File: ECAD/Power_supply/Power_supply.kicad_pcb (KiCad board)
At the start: 2 copper layers, 104 x 127 mm, 52 parts, among them J1 Barrel_Jack_Switch, J2 Conn_01x06, Q1 DMP3037LSS-13, SW1 SW_Push_DPDT, U1 LM317_TO-220, U2 LM317_TO-220, U3 LM317_TO-220

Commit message: Progressed ECAD.
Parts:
- moved C5 82.2 mm to (134.6, 153.7), turned to 0 degrees
- moved R2 69.9 mm to (141.0, 145.4), turned to 0 degrees
- moved C4 67.9 mm to (141.0, 142.9), turned to 0 degrees
- moved D6 66.6 mm to (134.6, 148.0)
- moved R5 64.7 mm to (134.6, 142.9), turned to 0 degrees
- moved C2 53.6 mm to (133.3, 136.5), turned to 90 degrees
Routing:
- net /ADJ_9V: track 18.4 -> 13.3 mm
- net GND: vias 14 -> 18
- added copper zone on F.Cu, net /ADJ_9V

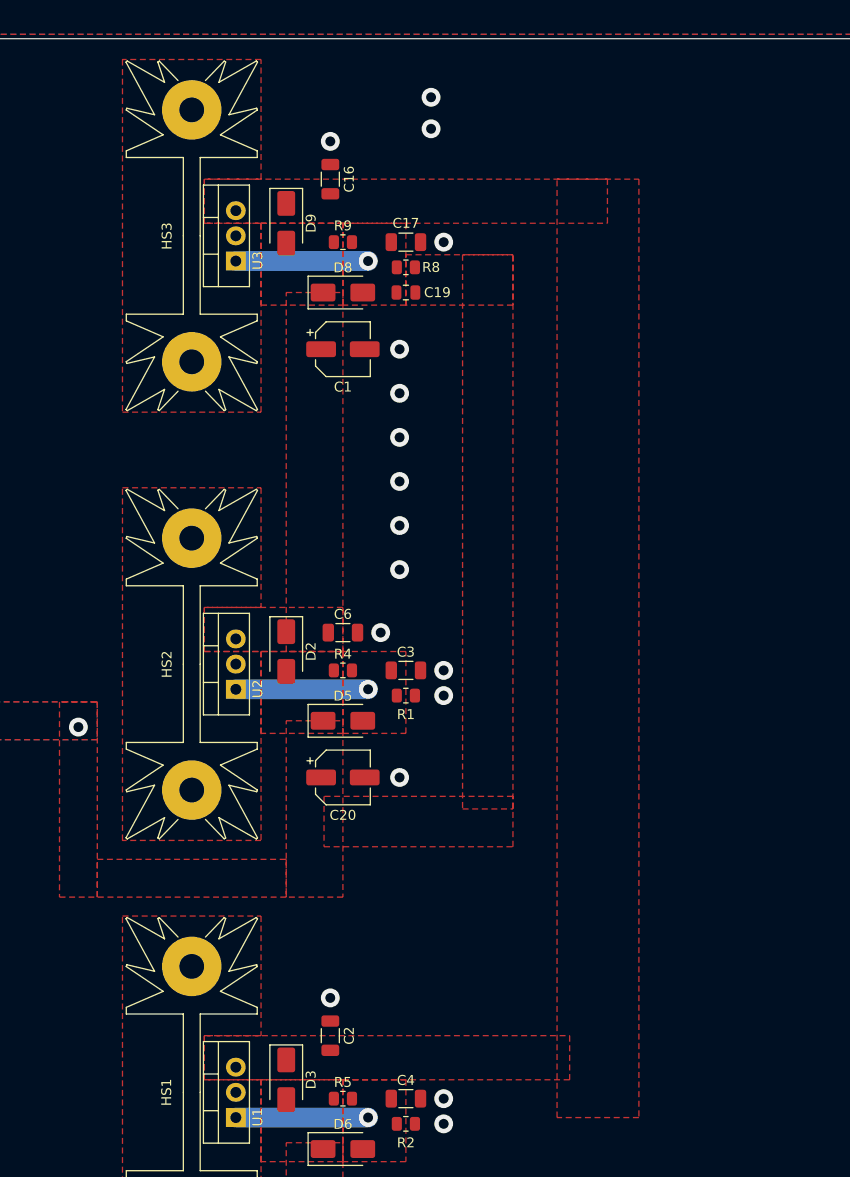
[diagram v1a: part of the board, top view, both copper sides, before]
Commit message: Improved layout.
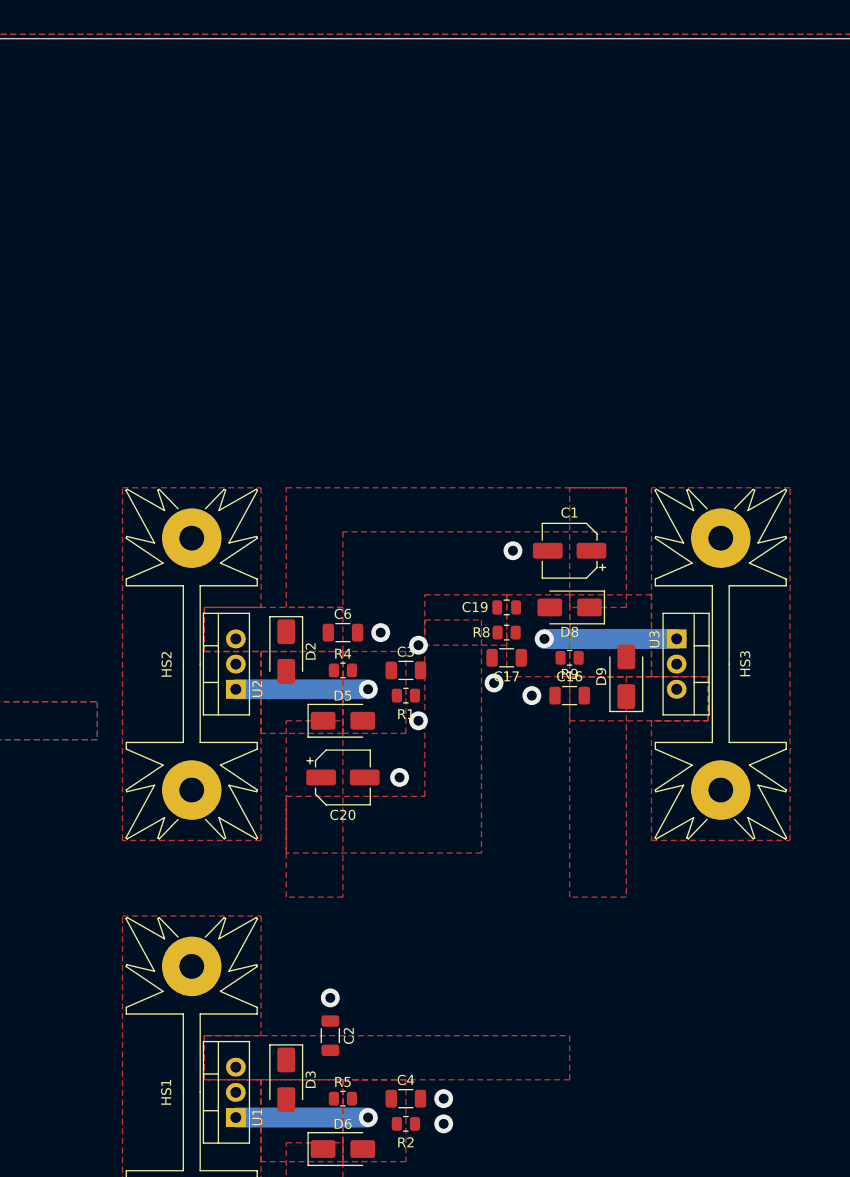
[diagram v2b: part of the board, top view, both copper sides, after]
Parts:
- moved HS3 68.6 mm to (172.7, 99.1), turned to -90 degrees
- moved U3 58.5 mm to (168.3, 96.5), turned to -90 degrees
- moved C16 57.4 mm to (157.5, 102.2), turned to 180 degrees
- moved D9 57.1 mm to (163.2, 100.3), turned to 90 degrees
- moved R9 47.7 mm to (157.5, 98.4), turned to 180 degrees
- moved C17 43.1 mm to (151.1, 98.4), turned to 180 degrees
- moved D8 39.1 mm to (157.5, 93.3), turned to 180 degrees
- moved R8 38.2 mm to (151.1, 95.9), turned to 180 degrees
- moved C19 33.3 mm to (151.1, 93.3), turned to 180 degrees
- moved C1 30.6 mm to (157.5, 87.6), turned to 180 degrees
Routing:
- net GND: vias 18 -> 11
- net +5V: vias 1 -> 0

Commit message: Progressed ECAD.
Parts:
- moved R7 168.3 mm to (168.5, 159.4)
- moved D7 168.3 mm to (160.6, 156.8)
- moved D1 134.1 mm to (169.5, 110.5), turned to 90 degrees
- moved Q1 117.7 mm to (175.9, 110.5), turned to 90 degrees
- moved D4 111.1 mm to (181.3, 114.0), turned to -90 degrees
- moved R3 109.5 mm to (182.9, 108.0), turned to 90 degrees
- moved FL1 102.0 mm to (182.9, 125.0), turned to -90 degrees
- moved J1 77.0 mm to (175.6, 88.9)
- moved SW1 67.3 mm to (177.0, 100.3), turned to 0 degrees
- moved C11 41.1 mm to (216.3, 134.4)
- moved C12 41.1 mm to (216.3, 137.7)
- moved C9 41.1 mm to (215.3, 145.4)
- moved L1 41.1 mm to (250.3, 132.4)
- moved L2 41.1 mm to (242.1, 132.4)
- moved C10 41.1 mm to (229.1, 145.4)
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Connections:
- net Net-(D1-A2) renamed /SW_OUT
- net Net-(J1-Pad1) renamed /SW_IN
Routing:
- net GND: track 0.00 -> 25.0 mm, vias 11 -> 12
- net GNDPWR: vias 0 -> 3
- net +9V: vias 0 -> 1
- net +5V: vias 0 -> 1
- net +12V: vias 0 -> 1
- added copper zone on B.Cu, net +12V
- added copper zone on B.Cu, net +9V
- added copper zone on F.Cu, net /SW_IN
- added copper zone on F.Cu, net /SW_OUT
- added copper zone on B.Cu, net GNDPWR
- removed copper zone on F.Cu, net GND
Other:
- board size 104 x 127 mm -> 95 x 127 mm

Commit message: Progressed PCB
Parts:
- moved L1 78.3 mm to (172.1, 130.6)
- moved R6 72.4 mm to (163.2, 157.5)
- moved C14 62.8 mm to (163.2, 153.0)
- moved C13 62.7 mm to (163.2, 149.2)
- moved L2 61.7 mm to (180.3, 130.8)
- moved C15 60.0 mm to (163.2, 141.6)
- moved C11 54.3 mm to (163.2, 145.4)
- moved C10 53.5 mm to (175.9, 151.8), turned to 180 degrees
- moved C12 53.1 mm to (163.2, 137.8)
- moved C9 39.6 mm to (175.9, 141.0), turned to 180 degrees
- moved D7 31.9 mm to (192.4, 154.3)
- moved R7 28.4 mm to (196.8, 161.3)
- moved FL1 8.25 mm to (175.9, 120.7)
- moved H4 5.08 mm to (180.3, 158.8)
- moved R3 2.01 mm to (182.2, 109.9)
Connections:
- net Net-(D4-K) renamed /PRE_FILTER
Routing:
- net Net-(D4-A): track 0.00 -> 8.32 mm
- net GNDPWR: track 0.00 -> 7.27 mm, vias 3 -> 4
- net GND: track 25.0 -> 26.9 mm
- added copper zone on F.Cu, net /PRE_FILTER

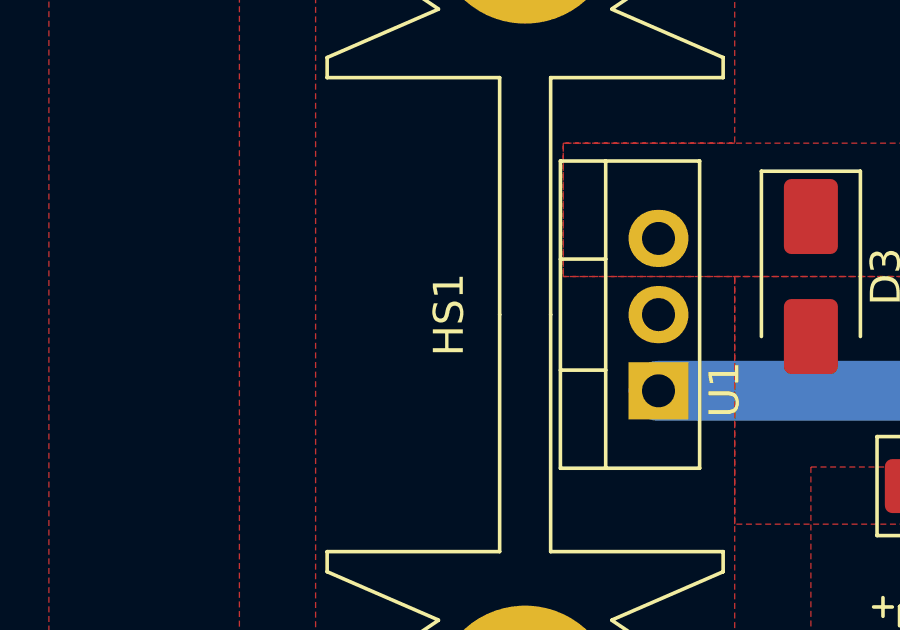
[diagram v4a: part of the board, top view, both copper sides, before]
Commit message: Added heatsink 3D model.
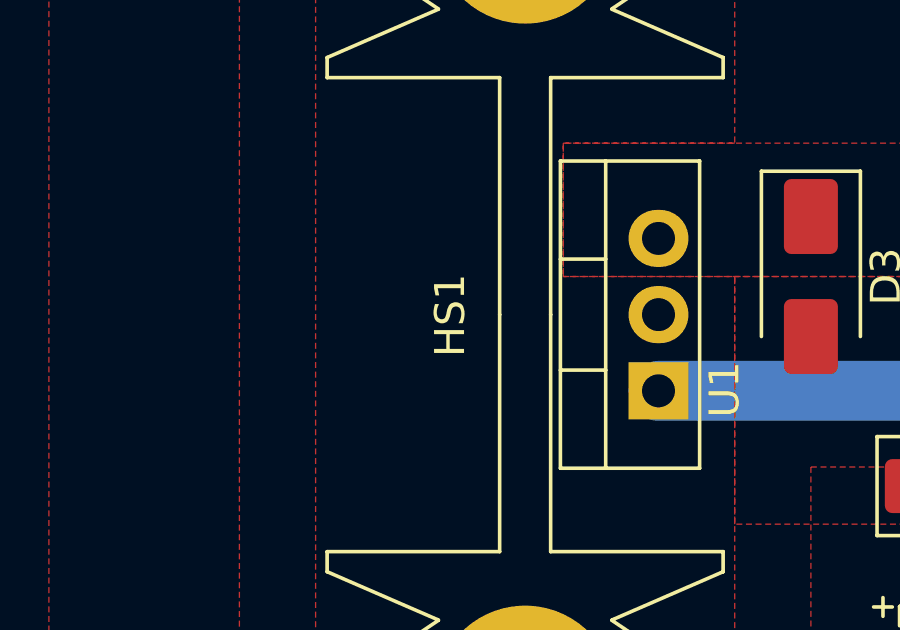
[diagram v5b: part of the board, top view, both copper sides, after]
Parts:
- HS1, HS2, HS3: footprint Heatsink:Heatsink_Fischer_SK104-STC-STIC_35x13mm_2xDrill2.5mm -> Heatsink_custom:Heatsink_Fischer_SK104-STC-STIC_35x13mm_2xDrill2.5mm
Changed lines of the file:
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@@
 		(tags "inductor taiyo-yuden nr smd")
 		(property "Reference" "L1"
-			(at 0 -4 360)
+			(at 0 -4 0)
 			(layer "F.SilkS")
 			(effects
@@
 		)
 		(property "Value" "100uL"
-			(at 0 4.5 360)
+			(at 0 4.5 0)
 			(layer "F.Fab")
 			(effects
@@
 		)
 		(fp_text user "${REFERENCE}"
-			(at 0 0 360)
+			(at 0 0 0)
 			(layer "F.Fab")
 			(effects
@@
 		(tags "inductor taiyo-yuden nr smd")
 		(property "Reference" "L2"
-			(at 0 -2.5 360)
+			(at 0 -2.5 0)
 			(layer "F.SilkS")
 			(effects
@@
 		)
 		(property "Value" "10uL"
-			(at 0 3 360)
+			(at 0 3 0)
 			(layer "F.Fab")
 			(effects
@@
 		)
 		(fp_text user "${REFERENCE}"
-			(at 0 0 360)
+			(at 0 0 0)
 			(layer "F.Fab")
 			(effects
@@
 		)
 	)
-	(footprint "Heatsink:Heatsink_Fischer_SK104-STC-STIC_35x13mm_2xDrill2.5mm"
+	(footprint "Heatsink_custom:Heatsink_Fischer_SK104-STC-STIC_35x13mm_2xDrill2.5mm"
 		(layer "F.Cu")
 		(at 119.38 137.16 90)
@@
 		(tags "Heatsink fischer TO-220")
 		(property "Reference" "HS1"
-			(at 0 -2.54 90)
+			(at -0.025 -2.5 90)
 			(layer "F.SilkS")
 			(effects
@@
 			)
 		)
-		(property "Footprint" "Heatsink:Heatsink_Fischer_SK104-STC-STIC_35x13mm_2xDrill2.5mm"
+		(property "Footprint" "Heatsink_custom:Heatsink_Fischer_SK104-STC-STIC_35x13mm_2xDrill2.5mm"
 			(at 0 0 90)
 			(unlocked yes)
@@
 			)
 		)
+		(model "/home/nunosousa/Git/SCART-switcher/CAD/sk_104_25.4_stc.igs"
+			(offset
+				(xyz -17.45 -6.359 0)
+			)
+			(scale
+				(xyz 1 1 1)
+			)
+			(rotate
+				(xyz 0 0 0)
+			)
+		)
 	)
 	(footprint "Capacitor_SMD:C_1206_3216Metric"
@@
 		)
 	)
-	(footprint "Heatsink:Heatsink_Fischer_SK104-STC-STIC_35x13mm_2xDrill2.5mm"
+	(footprint "Heatsink_custom:Heatsink_Fischer_SK104-STC-STIC_35x13mm_2xDrill2.5mm"
 		(layer "F.Cu")
 		(at 119.38 62.23 90)
@@
 			)
 		)
-		(property "Footprint" "Heatsink:Heatsink_Fischer_SK104-STC-STIC_35x13mm_2xDrill2.5mm"
+		(property "Footprint" "Heatsink_custom:Heatsink_Fischer_SK104-STC-STIC_35x13mm_2xDrill2.5mm"
 			(at 0 0 90)
 			(unlocked yes)
@@
 			)
 		)
+		(model "/home/nunosousa/Git/SCART-switcher/CAD/sk_104_25.4_stc.igs"
+			(offset
+				(xyz -17.45 -6.359 0)
+			)
+			(scale
+				(xyz 1 1 1)
+			)
+			(rotate
+				(xyz 0 0 0)
+			)
+		)
 	)
 	(footprint "Capacitor_SMD:C_1206_3216Metric"
@@
 		)
 	)
-	(footprint "Heatsink:Heatsink_Fischer_SK104-STC-STIC_35x13mm_2xDrill2.5mm"
+	(footprint "Heatsink_custom:Heatsink_Fischer_SK104-STC-STIC_35x13mm_2xDrill2.5mm"
 		(layer "F.Cu")
 		(at 172.72 62.23 -90)
@@
 		(tags "Heatsink fischer TO-220")
 		(property "Reference" "HS3"
-			(at -0.025 -2.5 90)
+			(at -0.025 -2.5 -90)
 			(layer "F.SilkS")
 			(effects
@@
 		)
 		(property "Value" "Heatsink"
-			(at 0.65 9.075 90)
+			(at 0.65 9.075 -90)
 			(layer "F.Fab")
 			(effects
@@
 			)
 		)
-		(property "Footprint" "Heatsink:Heatsink_Fischer_SK104-STC-STIC_35x13mm_2xDrill2.5mm"
+		(property "Footprint" "Heatsink_custom:Heatsink_Fischer_SK104-STC-STIC_35x13mm_2xDrill2.5mm"
 			(at 0 0 -90)
 			(unlocked yes)
@@
 		)
 		(fp_text user "${REFERENCE}"
-			(at 0 0 90)
+			(at 0 0 -90)
 			(layer "F.Fab")
 			(effects
@@
 			)
 			(scale
+				(xyz 1 1 1)
+			)
+			(rotate
+				(xyz 0 0 0)
+			)
+		)
+		(model "/home/nunosousa/Git/SCART-switcher/CAD/sk_104_25.4_stc.igs"
+			(offset
+				(xyz -17.45 -6.359 0)
+			)
+			(scale

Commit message: Progressed PCB.
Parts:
- moved D7 50.2 mm to (142.2, 155.6)
- moved R7 44.5 mm to (152.4, 159.4), turned to 180 degrees
- moved H1 12.0 mm to (107.0, 39.5)
- moved H3 12.0 mm to (107.0, 159.5)
- moved J2 9.06 mm to (106.7, 105.4)
- moved C12 5.68 mm to (160.7, 142.9)
- moved H2 5.36 mm to (182.5, 39.5)
- moved C15 4.58 mm to (160.7, 145.4)
- moved C11 3.59 mm to (160.7, 148.0)
- moved C13 2.84 mm to (160.7, 150.5)
- moved R6 2.84 mm to (160.7, 156.2)
- moved C14 2.54 mm to (160.7, 153.0)
- moved H4 2.29 mm to (182.5, 159.5)
- moved C10 0.63 mm to (175.9, 151.1)
- moved C9 0.63 mm to (175.9, 140.3)
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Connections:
- net Net-(FL1-Pad3) renamed /L1
- net Net-(L1-Pad2) renamed /L2
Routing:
- net Net-(D7-A): track 0.00 -> 7.74 mm
- net GND: track 26.9 -> 33.5 mm, vias 12 -> 20
- net GNDPWR: vias 4 -> 3
- added copper zone on F.Cu, net /L1
- added copper zone on F.Cu, net /L2
- added copper zone on F.Cu, net GND
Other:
- board size 95 x 127 mm -> 82.5 x 127 mm

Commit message: Progressed ECAD.
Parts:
- added J3: Conn_01x02, Connector_JST:JST_XH_B2B-XH-A_1x02_P2.50mm_Vertical, F.Cu at (168.5, 119.4)
- added REF**: Symbol_Barrel_Polarity, Symbol:Symbol_Barrel_Polarity, F.Cu at (182.9, 74.3)
- added REF**: KiCad-Logo2_5mm_SilkScreen, Symbol:KiCad-Logo2_5mm_SilkScreen, F.Cu at (144.8, 99.4)
- added kibuzzard-67A3D3AE: G***, kibuzzard-67A3D3AE, F.Cu at (113.7, 111.5)
- added kibuzzard-67B25D9F: G***, kibuzzard-67B25D9F, F.Cu at (182.9, 59.7)
- moved L1 0.38 mm to (172.1, 130.6)
- moved L2 0.38 mm to (180.3, 130.6)

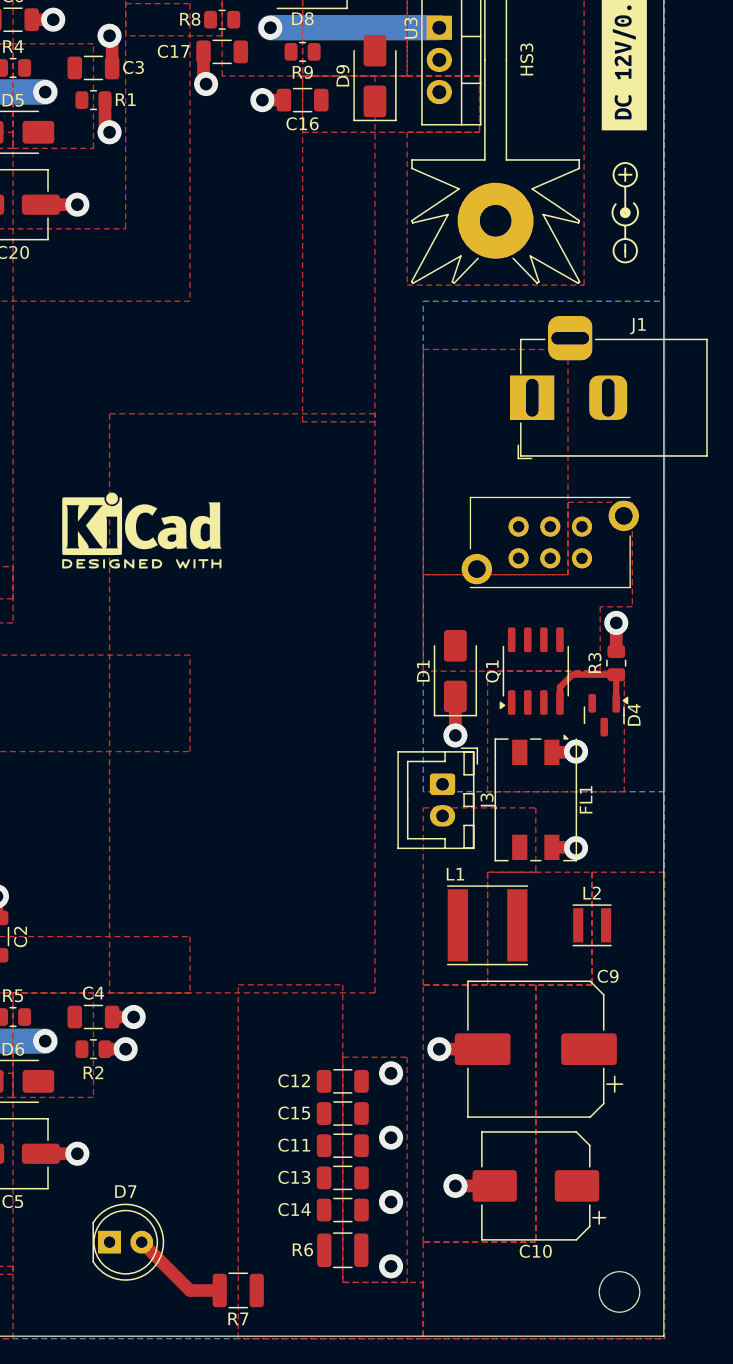
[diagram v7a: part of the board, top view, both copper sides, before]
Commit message: Added Fan.
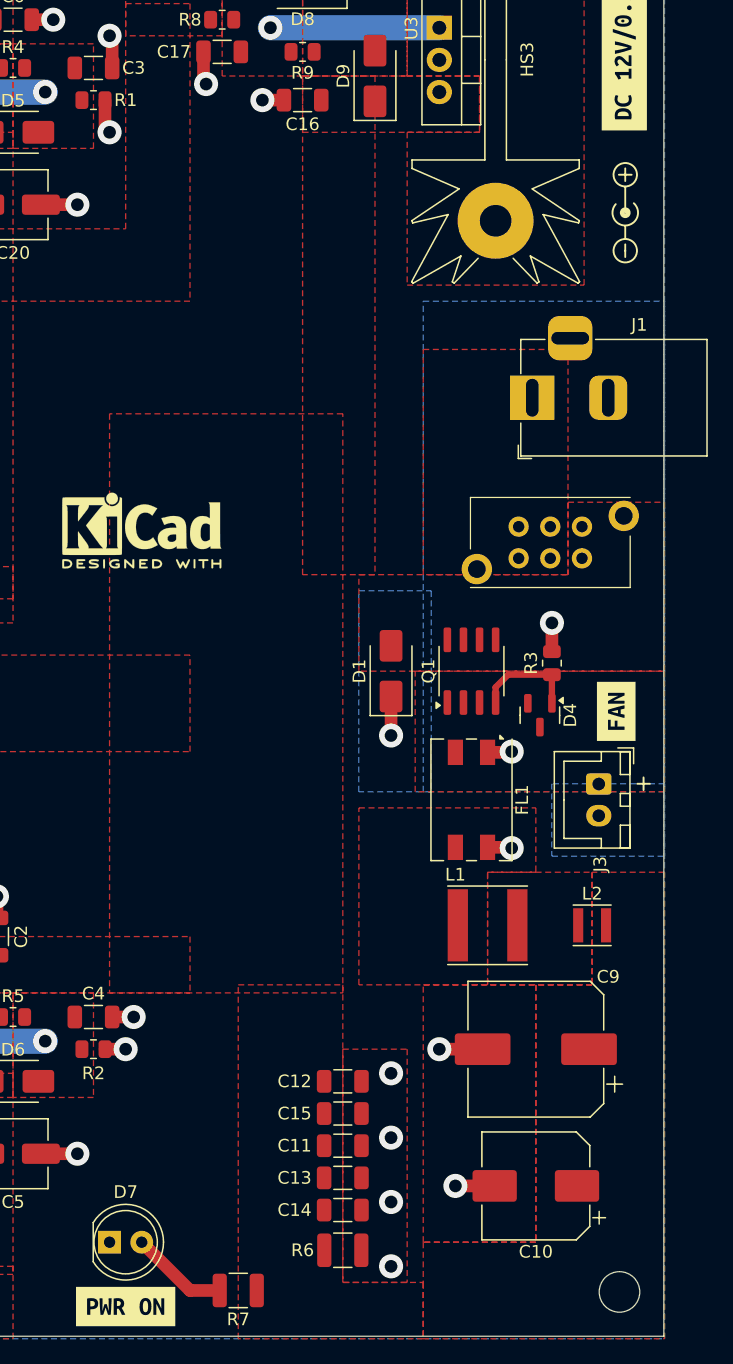
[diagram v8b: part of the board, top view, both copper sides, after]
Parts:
- added kibuzzard-67B5004D: G***, kibuzzard-67B5004D, F.Cu at (182.2, 113.7)
- added kibuzzard-67B50421: G***, kibuzzard-67B50421, F.Cu at (143.5, 160.7)
- moved J3 12.3 mm to (180.9, 119.4)
- moved FL1 5.08 mm to (170.8, 120.7)
- moved Q1 5.08 mm to (170.8, 110.5)
- moved R3 5.08 mm to (177.2, 109.9)
- moved D1 5.08 mm to (164.5, 110.5)
- moved D4 5.08 mm to (176.2, 114.0)
